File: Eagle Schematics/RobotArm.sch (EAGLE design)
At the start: 16 parts

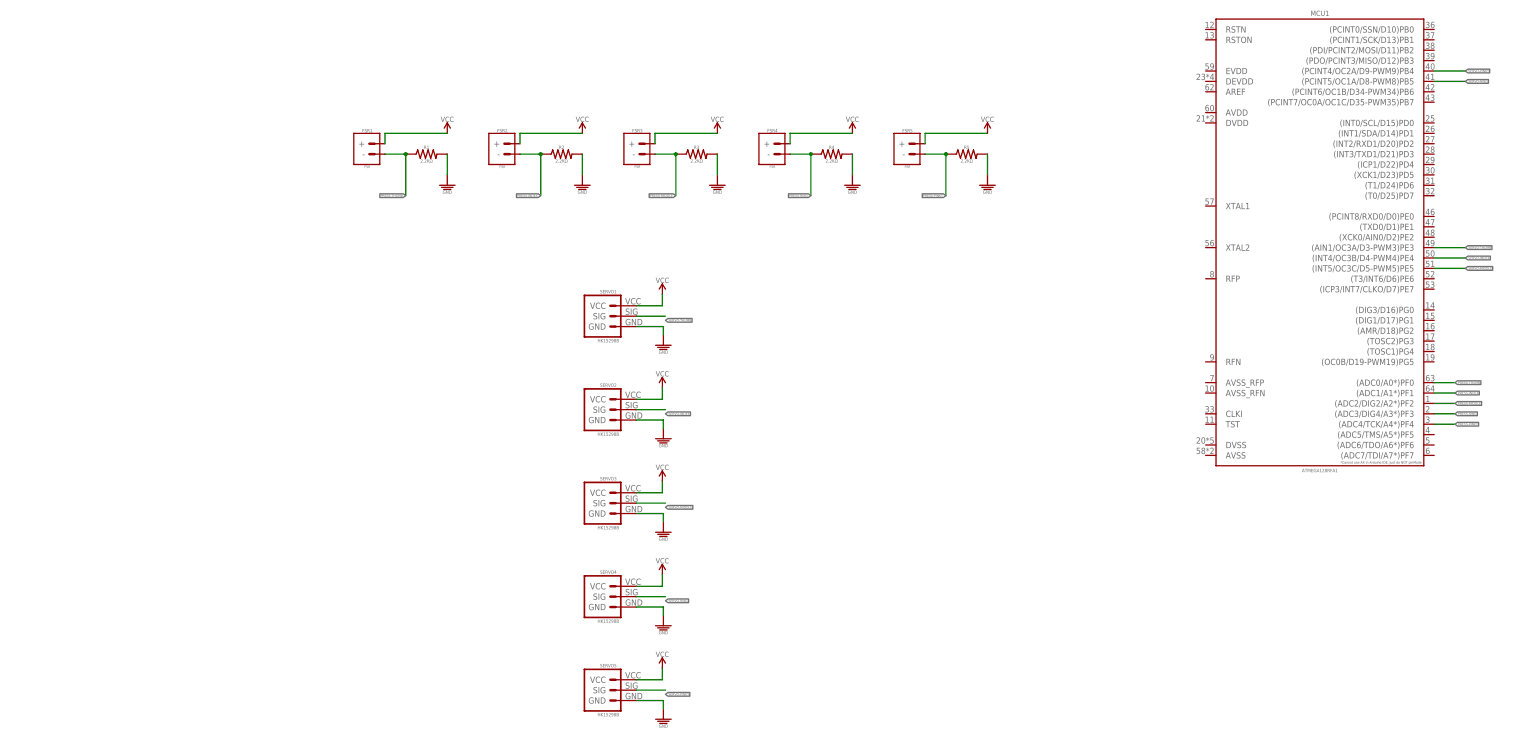
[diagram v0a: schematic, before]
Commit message: Updated RobotArm Schematic
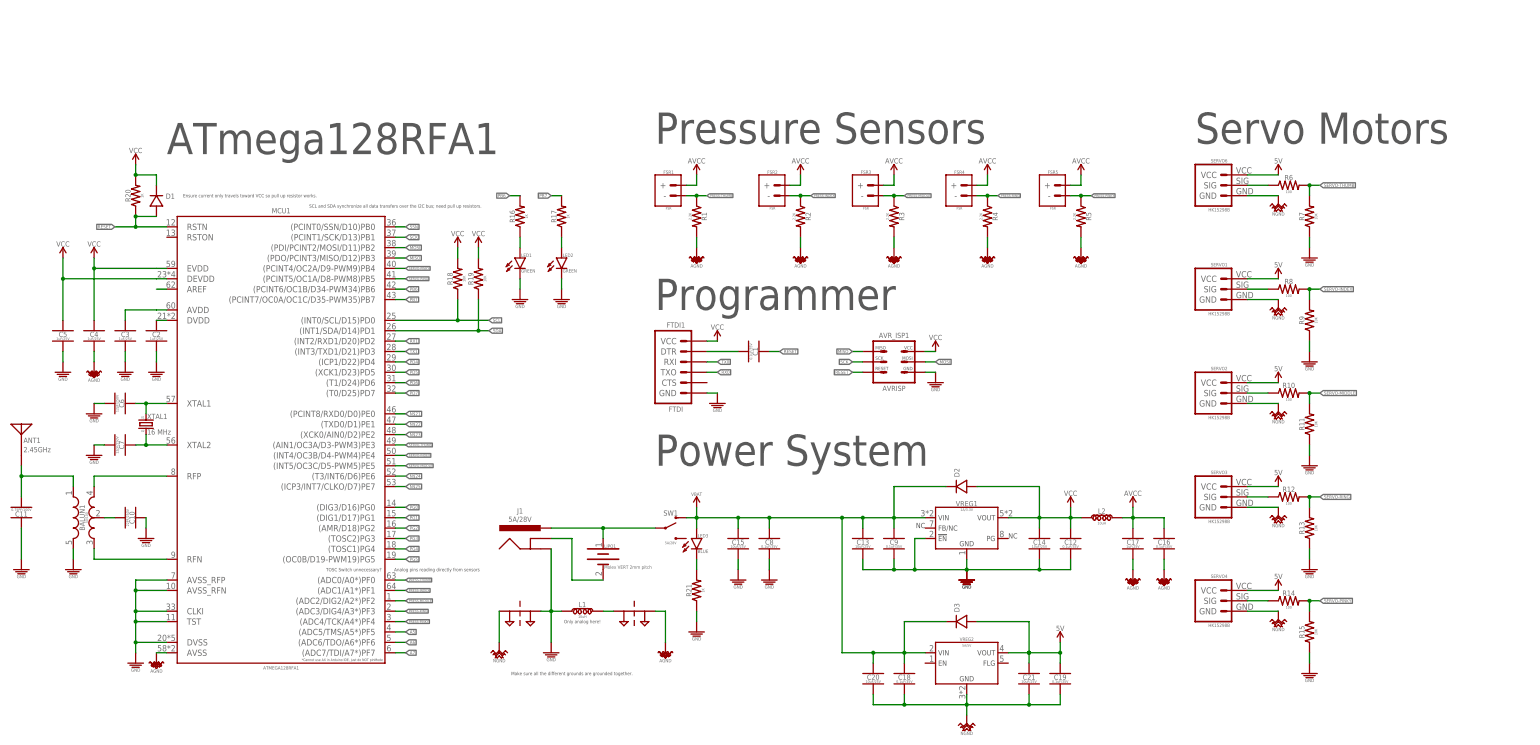
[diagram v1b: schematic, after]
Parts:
- removed SERVO5: HK15298B, PiB_motors:SERVO_SERVO-PN
- added ANT1: 2.45GHz, PiB_radio_frequency:ANTENNA_SMD_CHP-2.45GHZ-0.5DBI-3W
- added AVR_ISP1: AVRISP, PiB_connectors:AVR_SPI_PRG_6_PTH_VERT-MALE
- added BALUN1: 50/100, PiB_radio_frequency:BALUN_SMD-0805_UNBAL/BAL-50/100
- added C1, C12, C16, C18, C19, C8, C9: 0.1uF/35V, PiB_capacitors:0.1UF_SMD-0805_35V-10%
- added C10: 22PF/250V, PiB_capacitors:22PF_SMD-805_250V-5%
- added C11: 0.75PF/100V, PiB_capacitors:0.75PF_SMD-805_100V-33%
- added C13, C14, C15, C20, C21: 10uF/25V, PiB_capacitors:10UF_CER_SMD-0805_25V-10%
- added C17, C2, C3, C4, C5: 1uF/25V, PiB_capacitors:1UF_CER_SMD-0805_25V-10%
- added C6, C7: 12pF/250V, PiB_capacitors:12PF_SMD-0805_250V-5%
- added D1, D2, D3: (no value), PiB_discrete_semiconductors:DIODE_GENERAL-PURPOSE_SMD_GP_1A-50V
- added FTDI1: FTDI, PiB_connectors:FTDI_PTH_RA-MALE
- added J1: 5A/28V, PiB_connectors:POWER_JACK-BARREL_ID2.1MM-OD5.5MM_PTH_ID2.1MM-OD5.5MM
- added L1, L2: 10uH, PiB_inductors:10UH_SMD-805_0.5A-0.65OHM-10%
- added LED1, LED2: GREEN, PiB_leds:LED_SMD-0805_DISCRETE_GREEN_
- added LED3: BLUE, PiB_leds:LED_SMD-0805_DISCRETE_BLUE
- added LIPO1: Molex VERT 2mm pitch, PiB_connectors:1X02_MOLEX_89400_VERT-MALE_PITCH-2MM
- added NET_BRIDGE1, NET_BRIDGE2: 2PT_GND_TIE, PiB_power_symbols:2PT_GND_TIE
- added R10, R12, R14, R6, R8: 100, PiB_resistors:100Ω_SMD-0805_1/8W-5%
- added R11, R13, R15, R18, R19, R7, R9: 10K, PiB_resistors:10KΩ_SMD-0805_1/8W-5%
- added R16, R17, R20, R21: 1K, PiB_resistors:1KΩ_SMD-0805_1/8W-5%
- added SERVO6: HK15298B, PiB_motors:SERVO_SERVO-PN
- added SW1: 5A/28V, PiB_switches:SWITCH_SPDT_VERT_PTH_5A-28V_13L-7W_
- added VREG1: 1A/3.3V, PiB_ic_power:VREG_TPS768XX_ULDO_FAST-TRANSIENT_TPS76833QDR_1A-3.3V
- added VREG2: 5A/5V, PiB_ic_power:VREG_MIC29501-5.0_LINEAR_ULDO_5A-5V_MC29501-5.0_5A-5V
- added XTAL1: 16 MHz, PiB:CRYSTAL_ABM3B_16MHZ_18PF
- R1, R2, R3, R4, R5: value 2.2KΩ -> 2.2K
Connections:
- new net +: J1.PWR, LIPO1.+, SW1.P
- new net -: J1.GND@1, LIPO1.-
- new net 3.3V: AVR_ISP1.VCC
- new net 5V: C19.1, C21.1, D3.A, SERVO1.VCC, SERVO2.VCC, SERVO3.VCC, SERVO4.VCC, SERVO6.VCC, VREG2.VOUT
- new net A5: MCU1.(ADC5/TMS/A5*)PF5
- new net A6: MCU1.(ADC6/TDO/A6*)PF6
- new net A7: MCU1.(ADC7/TDI/A7*)PF7
- new net AGND: C16.2, C17.2, C4.2, MCU1.AVSS, NET_BRIDGE2.P$2
- new net AVCC: C16.1, C17.1, L2.2
- new net MISO: AVR_ISP1.MISO, MCU1.(PDO/PCINT3/MISO/D12)PB3
- new net MOSI: AVR_ISP1.MOSI, MCU1.(PDI/PCINT2/MOSI/D11)PB2
- new net N$1: R6.1, SERVO6.SIG
- new net N$10: C1.2, FTDI1.DTR
- new net N$11: BALUN1.OUT2, MCU1.RFP
- new net N$12: BALUN1.OUT1, MCU1.RFN
- new net N$13: MCU1.AREF
- new net N$14: C3.1, MCU1.AVDD
- new net N$15: C2.1, MCU1.DVDD
- new net N$16: BALUN1.GND@2, C10.2
- new net N$17: ANT1.SIGNAL, BALUN1.IN, C11.2
- new net N$19: L1.2, NET_BRIDGE2.P$1
- new net N$2: LED1.A, R16.1
- new net N$20: LED3.K, R21.2
- new net N$21: MCU1.(PCINT8/RXD0/D0)PE0
- new net N$22: MCU1.(TXD0/D1)PE1
- new net N$23: MCU1.(XCK0/AIN0/D2)PE2
- new net N$24: MCU1.(T3/INT6/D6)PE6
- new net N$25: MCU1.(ICP3/INT7/CLKO/D7)PE7
- new net N$3: R8.1, SERVO1.SIG
- new net N$4: R10.1, SERVO2.SIG
- new net N$5: R12.1, SERVO3.SIG
- new net N$6: R14.1, SERVO4.SIG
- new net N$7: LED2.A, R17.1
- new net N$8: C6.1, MCU1.XTAL1, XTAL1.XTAL1
- new net N$9: C7.1, MCU1.XTAL2, XTAL1.XTAL2
- new net NGND: C18.2, C19.2, C20.2, C21.2, NET_BRIDGE1.P$1, SERVO1.GND, SERVO2.GND, SERVO3.GND, SERVO4.GND, SERVO6.GND, VREG2.GND
- new net PB6: MCU1.(PCINT6/OC1B/D34-PWM34)PB6, R16.2
- new net PB7: MCU1.(PCINT7/OC0A/OC1C/D35-PWM35)PB7, R17.2
- new net PD4: MCU1.(ICP1/D22)PD4
- new net PD5: MCU1.(XCK1/D23)PD5
- new net PD6: MCU1.(T1/D24)PD6
- new net PD7: MCU1.(T0/D25)PD7
- new net PG0: MCU1.(DIG3/D16)PG0
- new net PG1: MCU1.(DIG1/D17)PG1
- new net PG2: MCU1.(AMR/D18)PG2
- new net PG3: MCU1.(TOSC2)PG3
- new net PG4: MCU1.(TOSC1)PG4
- new net PG5: MCU1.(OC0B/D19-PWM19)PG5
- new net RESET: AVR_ISP1.RESET, C1.1, D1.A, MCU1.RSTN, R20.1
- new net RX0: FTDI1.TXO
- new net RX1: MCU1.(INT2/RXD1/D20)PD2
- new net SCK: AVR_ISP1.SCK, MCU1.(PCINT1/SCK/D13)PB1
- new net SCL: MCU1.(INT0/SCL/D15)PD0, R18.1
- new net SDA: MCU1.(INT1/SDA/D14)PD1, R19.1
- new net SSN: MCU1.(PCINT0/SSN/D10)PB0
- new net TX0: FTDI1.RXI
- new net TX1: MCU1.(INT3/TXD1/D21)PD3
- new net VBAT: C13.1, C15.1, C18.1, C20.1, C8.1, C9.1, D2.K, D3.K, LED3.A, SW1.S1, VREG1.VIN, VREG2.VIN
- net GND: now also AVR_ISP1.GND, BALUN1.GND@5, C10.1, C11.1, C12.2, C13.2, C14.2, C15.2, C2.2, C3.2, C5.2, C6.2, C7.2, C8.2, C9.2, FTDI1.GND, J1.GND@2, L1.1, LED1.K, LED2.K, MCU1.AVSS_RFN, MCU1.AVSS_RFP, MCU1.CLKI, MCU1.DVSS, MCU1.TST, NET_BRIDGE1.P$2, R11.1, R13.1, R15.1, R21.1, R7.1, R9.1, VREG1.!EN, VREG1.GND; no longer SERVO1.GND, SERVO2.GND, SERVO3.GND, SERVO4.GND, SERVO5.GND
- net SERVO-INDEX: now also R8.2, R9.2; no longer SERVO2.SIG
- net SERVO-MIDDLE: now also R10.2, R11.2; no longer SERVO3.SIG
- net SERVO-PINKY: now also R14.2, R15.2; no longer SERVO5.SIG
- net SERVO-RING: now also R12.2, R13.2; no longer SERVO4.SIG
- net SERVO-THUMB: now also R6.2, R7.2; no longer SERVO1.SIG
- net VCC: now also C12.1, C14.1, C4.1, C5.1, D1.K, D2.A, FTDI1.VCC, L2.1, MCU1.DEVDD, MCU1.EVDD, R18.2, R19.2, R20.2, VREG1.VOUT; no longer SERVO1.VCC, SERVO2.VCC, SERVO3.VCC, SERVO4.VCC, SERVO5.VCC
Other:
- note added: "ATmega128RFA1"
- note added: "Analog pins reading directly from sensors"
- note added: "Ensure current only travels toward VCC so pull up resistor works."
- note added: "Make sure all the different grounds are grounded together."
- note added: "Only analog here!"
- note added: "Power System"
- note added: "Pressure Sensors"
- note added: "Programmer"
- note added: "SCL and SDA synchronize all data transfers over the I2C bus; need pull up resistors."
- note added: "Servo Motors"
- note added: "TOSC Switch unnecessary?"
- moved on the sheet: FSR1, FSR2, FSR3, FSR4, FSR5, MCU1, R1, R2, R3, R4, R5, SERVO1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

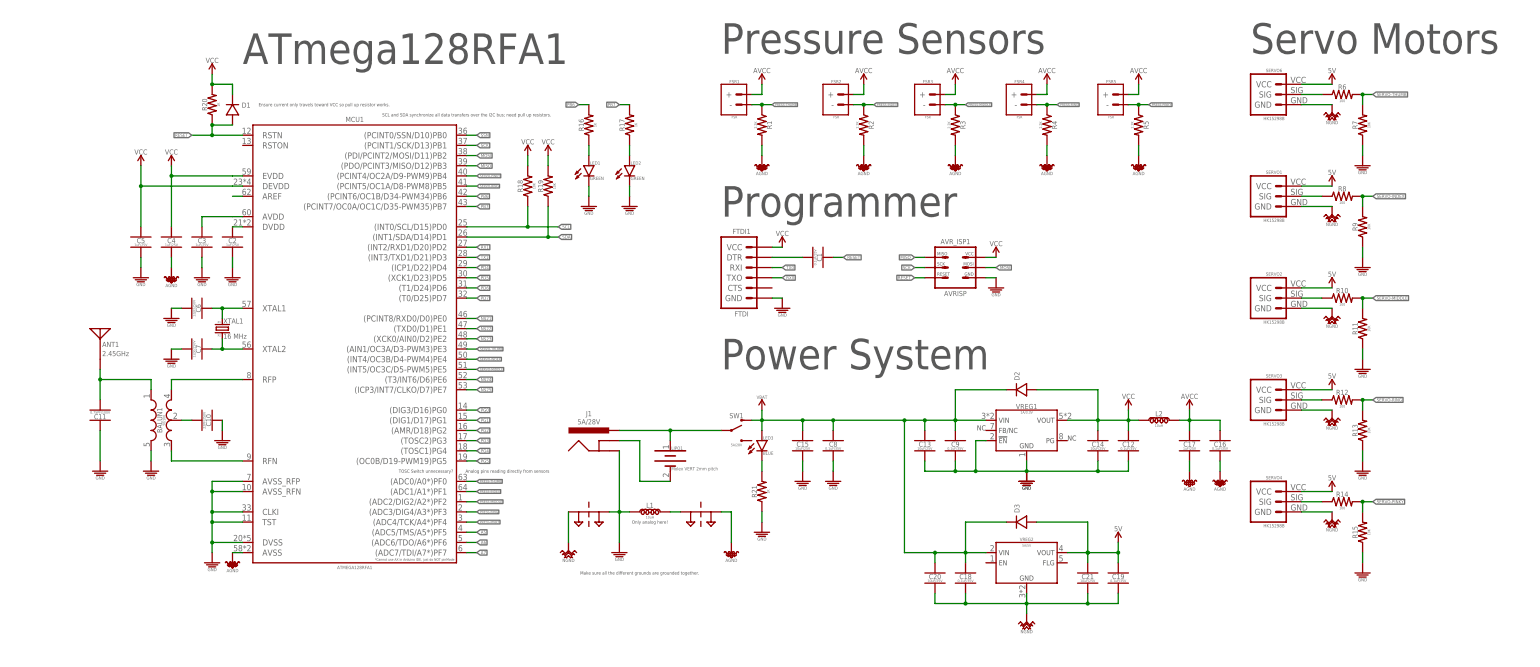
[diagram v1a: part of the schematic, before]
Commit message: Added so many capacitors it's not even funny
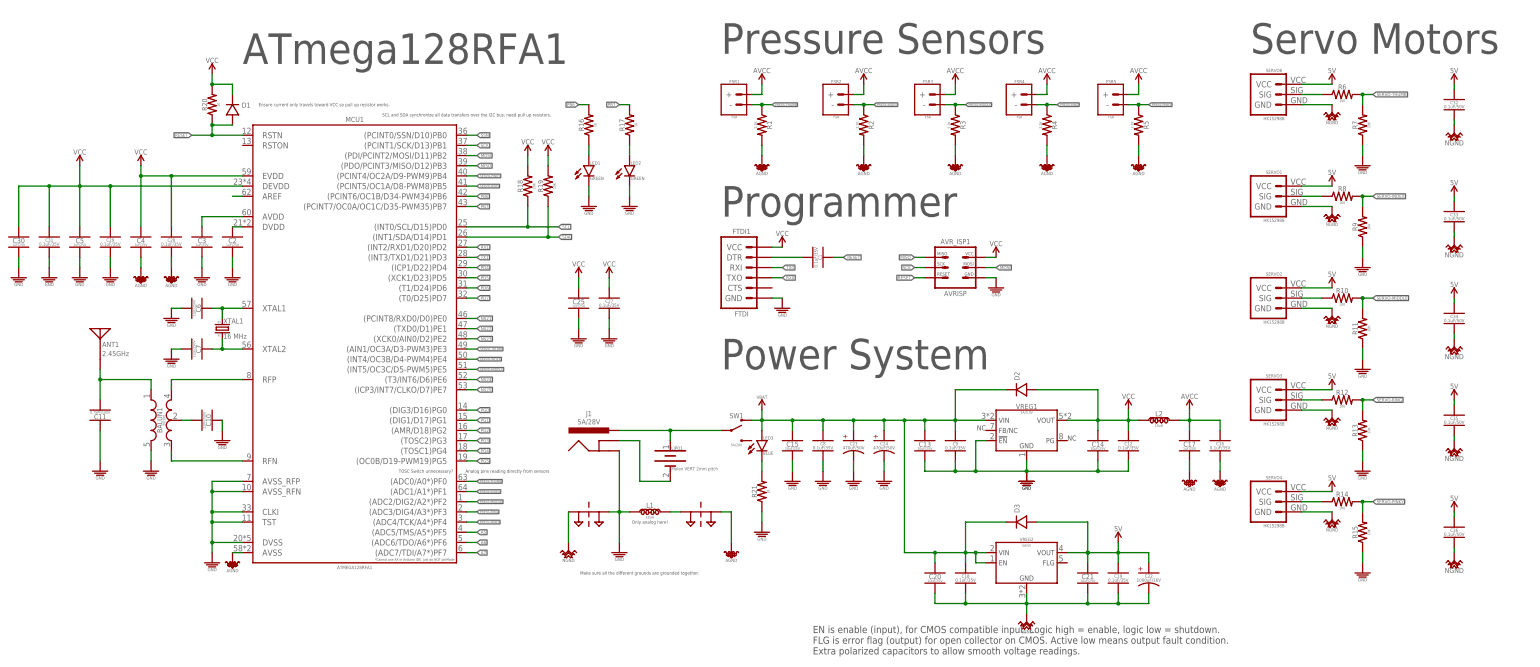
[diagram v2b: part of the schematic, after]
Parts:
- added C22: 1000uF/16V, PiB_capacitors:1000UF-POLARIZED_PTH_16V-20%
- added C23, C24: 470uF/50V, PiB_capacitors:470UF-POLARIZED
- added C25, C30: 1uF/25V, PiB_capacitors:1UF_CER_SMD-0805_25V-10%
- added C27, C28, C29, C31: 0.1uF/35V, PiB_capacitors:0.1UF_SMD-0805_35V-10%
- added C32, C33, C34, C35, C36: 0.1uF/50V, PiB_capacitors:0.1UF_SMD-0402_50V-10%
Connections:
- net 5V: now also C22.A, C32.1, C33.1, C34.1, C35.1, C36.1
- net AGND: now also C28.2
- net GND: now also C23.K, C24.K, C25.2, C27.2, C29.2, C30.2, C31.2
- net NGND: now also C22.K, C32.2, C33.2, C34.2, C35.2, C36.2
- net VBAT: now also C23.A, C24.A, VREG2.EN
- net VCC: now also C25.1, C27.1, C28.1, C29.1, C30.1, C31.1
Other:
- note added: "EN is enable (input), for CMOS compatible input. Logic high = enable, logic low = shutdown. FLG is error flag (output) for open collector on CMOS. Active low means output fault condition. Extra polarized capacitors to allow smooth voltage readings."
- moved on the sheet: C15, C4, C5, C8
